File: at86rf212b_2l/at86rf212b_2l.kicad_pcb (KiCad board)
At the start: 2 copper layers, 35 x 24.9 mm, 23 parts, among them J2 Conn_01x07, J3 Conn_01x07, U1 AT86RF212B, Y1 16.0Mhz

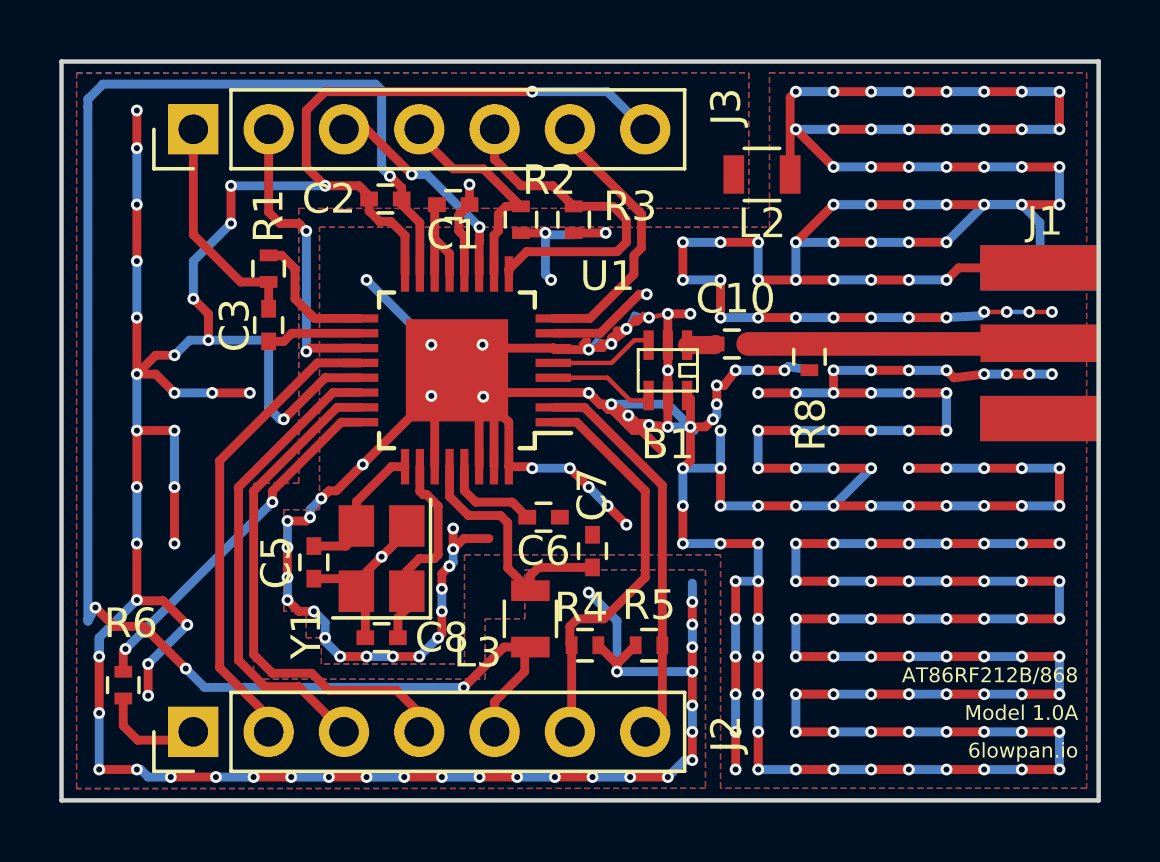
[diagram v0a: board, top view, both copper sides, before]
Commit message: Fix the Analog and Digital Ground connections for pins DIG1,DIG2,DIG3,DIG4. Were swapped in the previous version
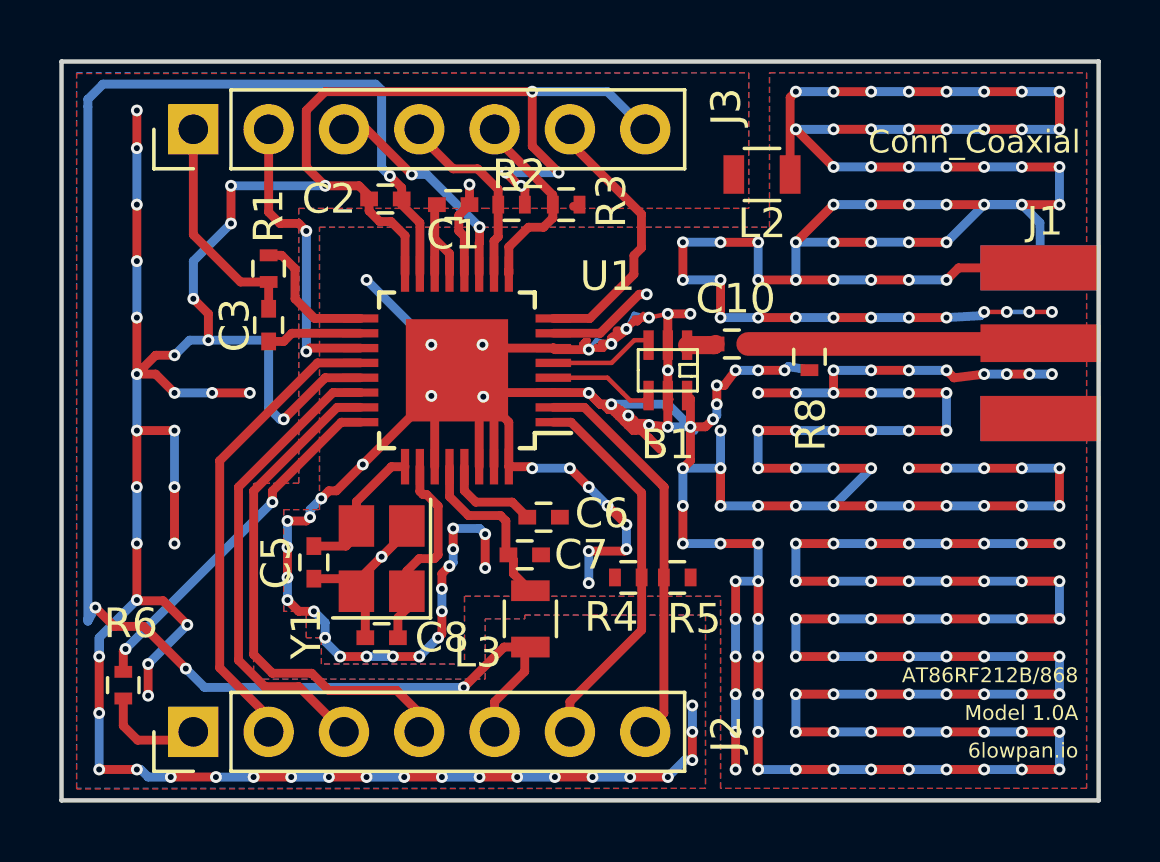
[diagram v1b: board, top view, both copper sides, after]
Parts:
- C5, C8: value 11pF -> 10pF
- J1: value (none) -> Conn_Coaxial
- moved R4 2.71 mm to (189.9, 88.8), turned to 0 degrees
- moved R5 2.48 mm to (191.6, 88.8), turned to 180 degrees
- moved C7 2.29 mm to (186.4, 88.0), turned to 180 degrees
- moved R2 0.60 mm to (186.0, 76.2), turned to 180 degrees
- moved R3 0.57 mm to (187.8, 76.2), turned to 180 degrees
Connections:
- J1 pad GND: GND -> (no net)
- R2 pad 1: GND -> GNDPWR
- R3 pad 1: GND -> GNDPWR
- R4 pad 1: GNDPWR -> GND
- R5 pad 1: GNDPWR -> GND
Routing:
- net GNDPWR: track 118.2 -> 112.7 mm, vias 55 -> 52
- net /DIG1: track 11.6 -> 6.75 mm
- net VDD: track 8.66 -> 5.94 mm
- net /DIG2: track 7.57 -> 6.52 mm
- net /DIG3: track 13.9 -> 13.2 mm
- net GND: track 329.2 -> 328.8 mm, vias 224 -> 226

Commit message: latest fixes on vias, layers, pads for the SMA antenna and the edge cuts area.
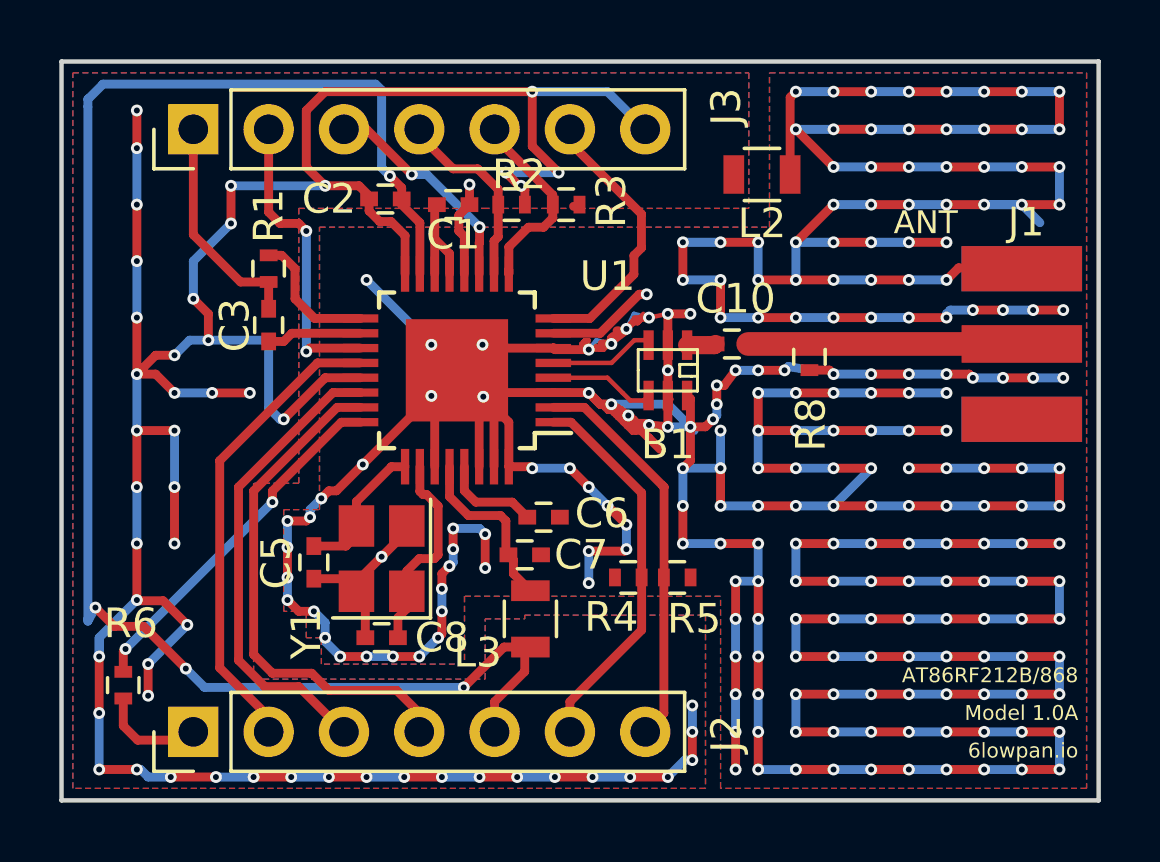
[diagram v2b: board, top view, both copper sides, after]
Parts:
- J1: value Conn_Coaxial -> ANT
- moved J1 0.64 mm to (205.2, 80.9)
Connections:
- J1 pad GND: (no net) -> GND
- J1 pad P: (no net) -> Net-(C10-Pad1)
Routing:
- net GND: track 328.8 -> 326.4 mm
